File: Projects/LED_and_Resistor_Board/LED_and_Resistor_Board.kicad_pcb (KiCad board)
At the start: 2 copper layers, 41.9 x 12.7 mm, 3 parts

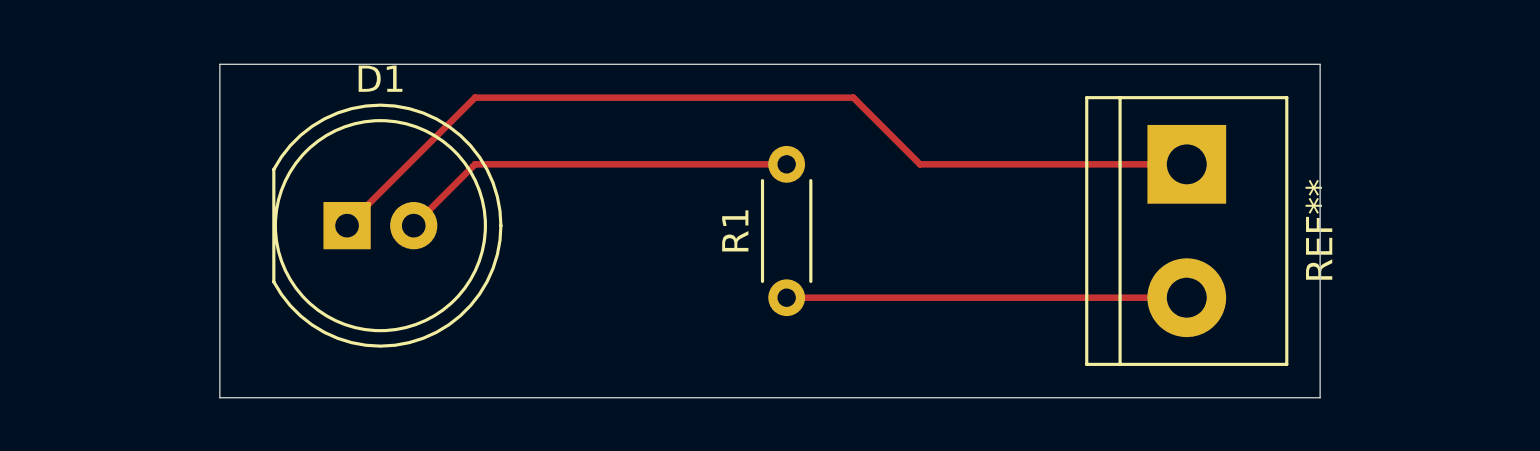
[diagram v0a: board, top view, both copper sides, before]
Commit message: Round PCB edges and add mounting holes
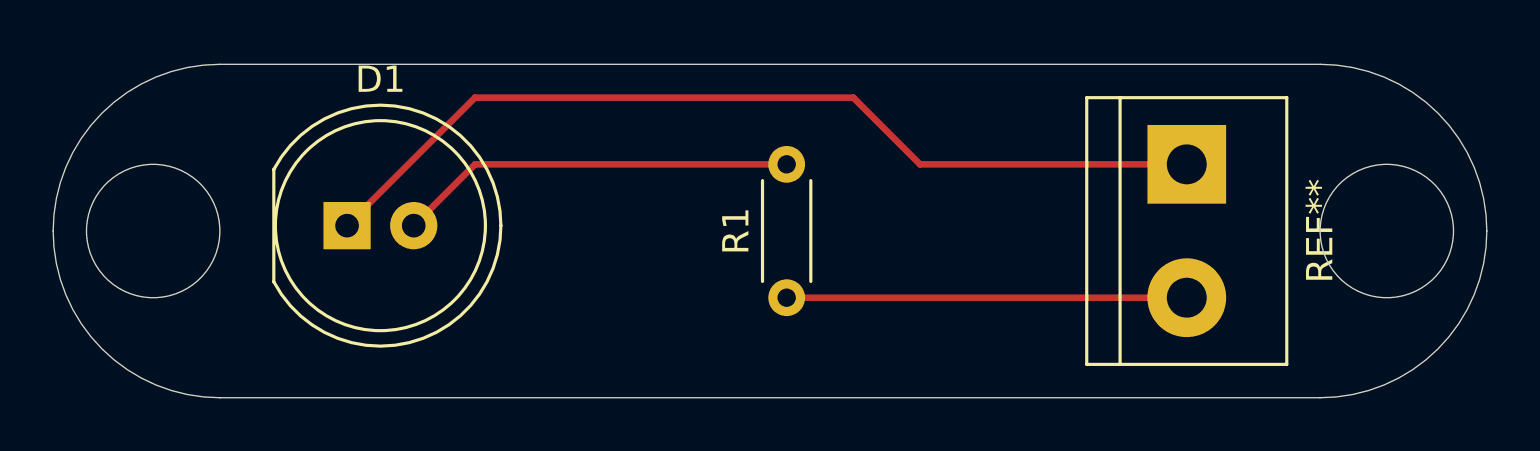
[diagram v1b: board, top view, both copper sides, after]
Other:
- board size 41.9 x 12.7 mm -> 54.6 x 12.7 mm
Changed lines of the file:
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@@
   (general
     (thickness 1.6)
-    (drawings 4)
+    (drawings 8)
     (tracks 7)
     (zones 0)
@@
     )
   )
-  (gr_line (start 177.8 105.41) (end 177.8 92.71) (angle 90) (layer Edge.Cuts) (width 0.05))
+  (gr_circle (center 180.34 99.06) (end 182.88 99.06) (layer Edge.Cuts) (width 0.05))
+  (gr_circle (center 133.35 99.06) (end 135.89 99.06) (layer Edge.Cuts) (width 0.05))
+  (gr_arc (start 135.89 99.06) (end 135.89 105.41) (angle 90) (layer Edge.Cuts) (width 0.05))
+  (gr_arc (start 135.89 99.06) (end 129.54 99.06) (angle 90) (layer Edge.Cuts) (width 0.05))
+  (gr_arc (start 177.8 99.06) (end 184.15 99.06) (angle 90) (layer Edge.Cuts) (width 0.05))
+  (gr_arc (start 177.8 99.06) (end 177.8 92.71) (angle 90) (layer Edge.Cuts) (width 0.05))
   (gr_line (start 135.89 105.41) (end 177.8 105.41) (angle 90) (layer Edge.Cuts) (width 0.05))
-  (gr_line (start 135.89 92.71) (end 135.89 105.41) (angle 90) (layer Edge.Cuts) (width 0.05))
   (gr_line (start 177.8 92.71) (end 135.89 92.71) (angle 90) (layer Edge.Cuts) (width 0.05))
   (segment (start 173.355 96.52) (end 162.56 96.52) (width 0.25) (layer F.Cu) (net 1) (status 400000))

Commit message: Fill F.Cu layer - 5V, thermal reliefs
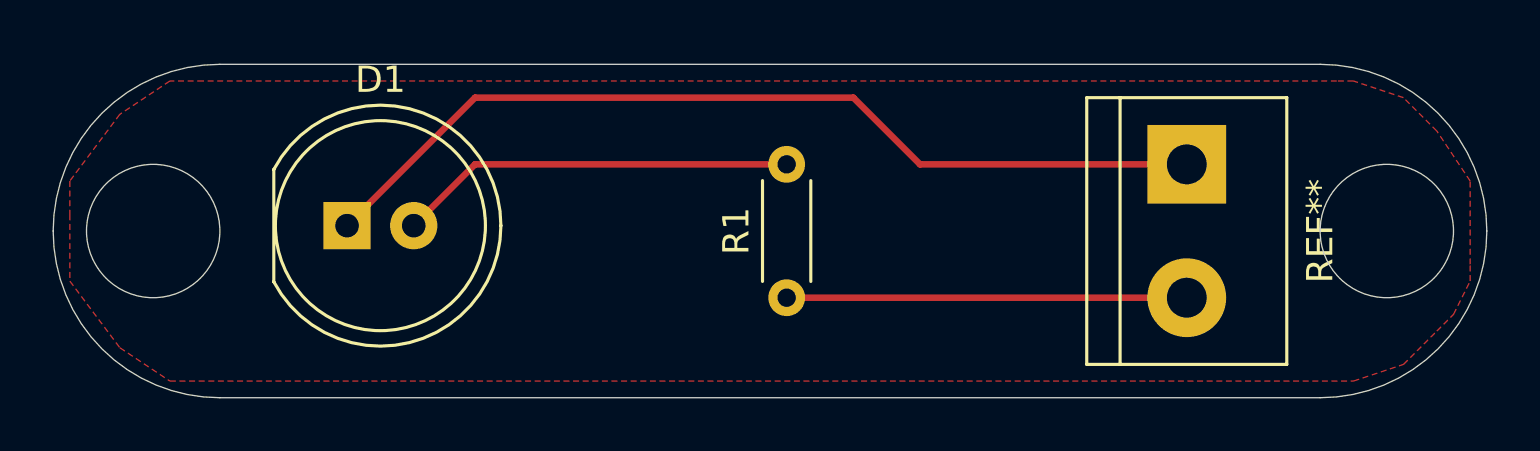
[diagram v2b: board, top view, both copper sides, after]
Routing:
- added copper zone on F.Cu, net +5V
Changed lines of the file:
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@@
   (segment (start 157.48 96.52) (end 145.610002 96.52) (width 0.25) (layer F.Cu) (net 2))
   (segment (start 157.48 101.6) (end 173.355 101.6) (width 0.25) (layer F.Cu) (net 3) (status C00000))
+  (zone (net 3) (net_name +5V) (layer F.Cu) (hatch edge 0.508)
+    (connect_pads (clearance 0.508))
+    (min_thickness 0.254)
+    (fill yes (arc_segments 32) (thermal_gap 0.508) (thermal_bridge_width 0.508))
+    (polygon
+      (pts
+        (xy 178.435 93.345) (xy 135.255 93.345) (xy 133.985 93.345) (xy 132.08 94.615) (xy 130.175 97.155)
+        (xy 130.175 98.425) (xy 130.175 100.965) (xy 132.08 103.505) (xy 133.985 104.775) (xy 179.07 104.775)
+        (xy 180.975 104.14) (xy 182.245 102.87) (xy 182.88 102.235) (xy 183.515 100.965) (xy 183.515 100.33)
+        (xy 183.515 97.155) (xy 182.245 95.25) (xy 180.975 93.98) (xy 179.07 93.345)
+      )
+    )
+  )
 )

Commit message: Add silkscreen print and dimensions
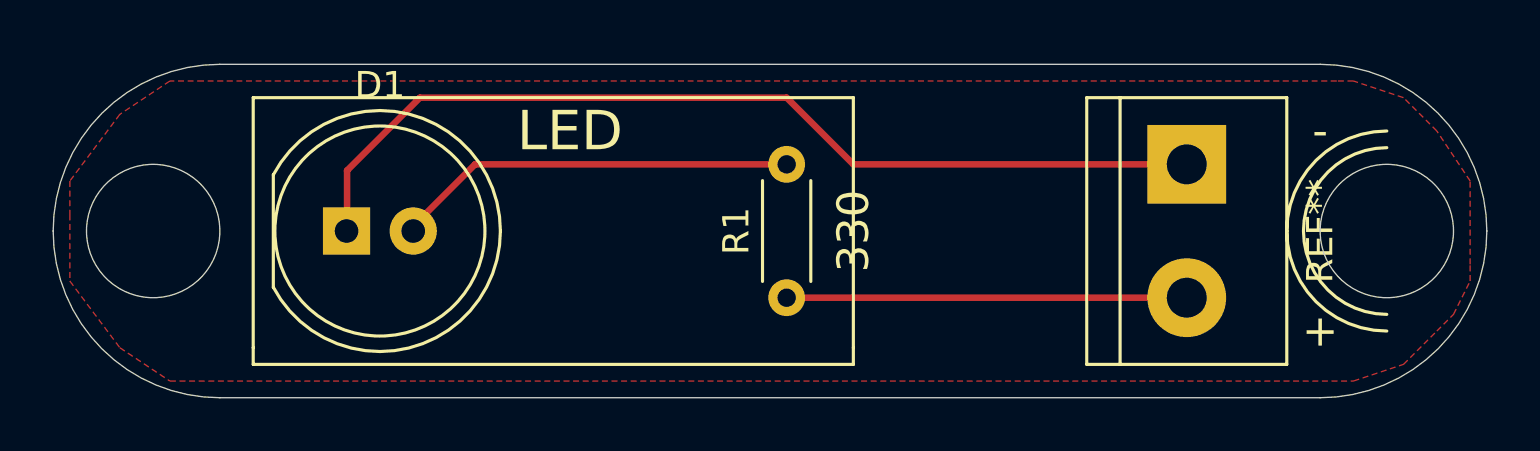
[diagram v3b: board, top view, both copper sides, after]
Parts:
- added REF**: OSHW-Logo2_7.3x6mm_SilkScreen, Symbol:OSHW-Logo2_7.3x6mm_SilkScreen, B.Cu at (164.5, 99.1)
- moved D1 0.21 mm to (140.7, 99.1)
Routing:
- net (no net): track 0.00 -> 36.3 mm
- net GND: track 35.7 -> 0.00 mm
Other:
- board text added: "+"
- board text added: "-"
- board text added: "330"
- board text added: "LED"
- board text added: "Simple LED & Resistor PCB Version 1 December 6, 2021 Designed by Michael Ly"

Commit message: Add header to Schematic and change PCB - no more DRC errors
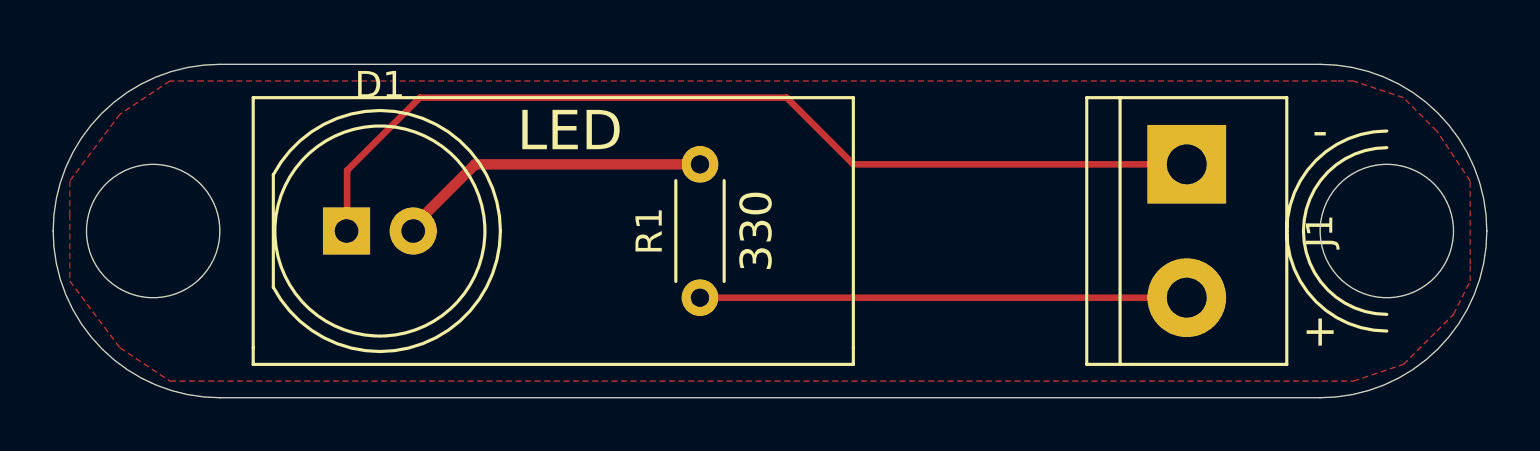
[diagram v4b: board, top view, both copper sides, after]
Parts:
- removed the REF** at (172.7, 96.5)
- added J1: Conn_01x02_Male, TerminalBlock:TerminalBlock_bornier-2_P5.08mm, F.Cu at (172.7, 96.5)
- moved R1 3.30 mm to (154.2, 101.6)
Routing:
- net GND: track 0.00 -> 36.3 mm
- net (no net): track 36.3 -> 0.00 mm
- net Net-(D1-Pad2): track 15.2 -> 11.9 mm
- net +5V: track 15.9 -> 18.5 mm
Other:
- net class PWR added: clearance 0.2, trace_width 0.4, via_dia 0.8, via_drill 0.4
